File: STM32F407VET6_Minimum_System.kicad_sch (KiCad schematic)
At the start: 20 parts, among them SW1 SW_DIP_x01, U1 STM32F407VET, Y1 8MHz

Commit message: feat: implement sensors schematic
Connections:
- net DHT_DATA_MCU: now reaches U1.84 (PD3)
- net SENS_SCL: now reaches U1.95 (PB8)
- net SENS_SDA: now reaches U1.96 (PB9)
- net BTN1_N: no longer names the net of U1.97 (PE0)
- net BTN2_N: no longer names the net of U1.98 (PE1)
- net LED_1: no longer names the net of U1.1 (PE2)
- net LED_2: no longer names the net of U1.2 (PE3)
- net LED_3: no longer names the net of U1.3 (PE4)
- net LED_4: no longer names the net of U1.4 (PE5)
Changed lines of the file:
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@@
+	(wire
+		(pts
+			(xy 173.99 124.46) (xy 180.34 124.46)
+		)
+		(stroke
+			(width 0)
+			(type default)
+		)
+	)
 	(wire
 		(pts
@@
 	(wire
 		(pts
-			(xy 170.18 86.36) (xy 180.34 86.36)
-		)
-		(stroke
-			(width 0)
-			(type default)
-		)
-	)
-	(wire
-		(pts
 			(xy 167.64 50.8) (xy 180.34 50.8)
 		)
@@
 	(wire
 		(pts
+			(xy 231.14 114.3) (xy 238.76 114.3)
+		)
+		(stroke
+			(width 0)
+			(type default)
+		)
+	)
+	(wire
+		(pts
 			(xy 203.2 34.29) (xy 205.74 34.29)
 		)
@@
 	(wire
 		(pts
-			(xy 170.18 81.28) (xy 180.34 81.28)
-		)
-		(stroke
-			(width 0)
-			(type default)
-		)
-	)
-	(wire
-		(pts
 			(xy 76.2 121.92) (xy 80.01 121.92)
 		)
@@
 	(wire
 		(pts
-			(xy 171.45 73.66) (xy 180.34 73.66)
-		)
-		(stroke
-			(width 0)
-			(type default)
-		)
-	)
-	(wire
-		(pts
 			(xy 331.47 149.86) (xy 331.47 146.05)
 		)
@@
 	(wire
 		(pts
-			(xy 231.14 93.98) (xy 242.57 93.98)
-		)
-		(stroke
-			(width 0)
-			(type default)
-		)
-	)
-	(wire
-		(pts
 			(xy 208.28 185.42) (xy 208.28 189.23)
 		)
@@
 	(wire
 		(pts
-			(xy 170.18 78.74) (xy 180.34 78.74)
-		)
-		(stroke
-			(width 0)
-			(type default)
-		)
-	)
-	(wire
-		(pts
 			(xy 328.93 97.79) (xy 328.93 92.71)
 		)
@@
 	(wire
 		(pts
-			(xy 172.72 111.76) (xy 180.34 111.76)
-		)
-		(stroke
-			(width 0)
-			(type default)
-		)
-	)
-	(wire
-		(pts
 			(xy 96.52 162.56) (xy 104.14 162.56)
 		)
@@
 	(wire
 		(pts
-			(xy 171.45 76.2) (xy 180.34 76.2)
-		)
-		(stroke
-			(width 0)
-			(type default)
-		)
-	)
-	(wire
-		(pts
 			(xy 64.77 121.92) (xy 68.58 121.92)
 		)
@@
 	(wire
 		(pts
-			(xy 170.18 83.82) (xy 180.34 83.82)
-		)
-		(stroke
-			(width 0)
-			(type default)
-		)
-	)
-	(wire
-		(pts
 			(xy 215.9 31.75) (xy 215.9 40.64)
+		)
+		(stroke
+			(width 0)
+			(type default)
+		)
+	)
+	(wire
+		(pts
+			(xy 231.14 116.84) (xy 238.76 116.84)
 		)
 		(stroke
@@
 		)
 	)
+	(label "USB_D_N"
+		(at 242.57 78.74 0)
+		(effects
+			(font
+				(size 1.27 1.27)
+			)
+			(justify left bottom)
+		)
+	)
 	(label "PH1"
 		(at 170.18 68.58 0)
@@
 		)
 	)
-	(global_label "LED_1"
-		(shape input)
-		(at 170.18 78.74 180)
-		(fields_autoplaced yes)
-		(effects
-			(font
-				(size 1.27 1.27)
-			)
-			(justify right)
-		)
-		(property "Intersheetrefs" "${INTERSHEET_REFS}"
-			(at 161.5706 78.74 0)
-			(hide yes)
-			(show_name no)
-			(do_not_autoplace no)
-			(effects
-				(font
-					(size 1.27 1.27)
-				)
-				(justify right)
-			)
+	(label "USB_D_P"
+		(at 242.57 81.28 0)
+		(effects
+			(font
+				(size 1.27 1.27)
+			)
+			(justify left bottom)
 		)
 	)
@@
 		)
 	)
-	(global_label "USB_D_N"
+	(global_label "SENS_SCL"
 		(shape input)
-		(at 242.57 78.74 0)
+		(at 238.76 114.3 0)
 		(fields_autoplaced yes)
 		(effects
@@
 		)
 		(property "Intersheetrefs" "${INTERSHEET_REFS}"
-			(at 253.9009 78.74 0)
+			(at 251.1189 114.3 0)
 			(hide yes)
 			(show_name no)
@@
 				)
 				(justify left)
-			)
-		)
-	)
-	(global_label "BTN1_N"
-		(shape input)
-		(at 171.45 73.66 180)
-		(fields_autoplaced yes)
-		(effects
-			(font
-				(size 1.27 1.27)
-			)
-			(justify right)
-		)
-		(property "Intersheetrefs" "${INTERSHEET_REFS}"
-			(at 161.3891 73.66 0)
-			(hide yes)
-			(show_name no)
-			(do_not_autoplace no)
-			(effects
-				(font
-					(size 1.27 1.27)
-				)
-				(justify right)
-			)
-		)
-	)
-	(global_label "BTN2_N"
-		(shape input)
-		(at 171.45 76.2 180)
-		(fields_autoplaced yes)
-		(effects
-			(font
-				(size 1.27 1.27)
-			)
-			(justify right)
-		)
-		(property "Intersheetrefs" "${INTERSHEET_REFS}"
-			(at 161.3891 76.2 0)
-			(hide yes)
-			(show_name no)
-			(do_not_autoplace no)
-			(effects
-				(font
-					(size 1.27 1.27)
-				)
-				(justify right)
-			)
-		)
-	)
-	(global_label "LED_3"
-		(shape input)
-		(at 170.18 83.82 180)
-		(fields_autoplaced yes)
-		(effects
-			(font
-				(size 1.27 1.27)
-			)
-			(justify right)
-		)
-		(property "Intersheetrefs" "${INTERSHEET_REFS}"
-			(at 161.5706 83.82 0)
-			(hide yes)
-			(show_name no)
-			(do_not_autoplace no)
-			(effects
-				(font
-					(size 1.27 1.27)
-				)
-				(justify right)
 			)
 		)
@@
 		)
 	)
-	(global_label "USB_D_P"
+	(global_label "SENS_SDA"
 		(shape input)
-		(at 242.57 81.28 0)
+		(at 238.76 116.84 0)
 		(fields_autoplaced yes)
 		(effects
@@
 		)
 		(property "Intersheetrefs" "${INTERSHEET_REFS}"
-			(at 253.8404 81.28 0)
+			(at 251.1794 116.84 0)
 			(hide yes)
 			(show_name no)
@@
 		)
 	)
-	(global_label "LED_4"
+	(global_label "DHT_DATA_MCU"
 		(shape input)
-		(at 170.18 86.36 180)
+		(at 173.99 124.46 180)
 		(fields_autoplaced yes)
 		(effects
@@
 		)
 		(property "Intersheetrefs" "${INTERSHEET_REFS}"
-			(at 161.5706 86.36 0)
+			(at 157.0348 124.46 0)
 			(hide yes)
 			(show_name no)
-			(do_not_autoplace no)
-			(effects
-				(font
-					(size 1.27 1.27)
-				)
-				(justify right)
-			)
-		)
-	)
-	(global_label "LED_2"
-		(shape input)
-		(at 170.18 81.28 180)
-		(fields_autoplaced yes)
-		(effects
-			(font
-				(size 1.27 1.27)
-			)
-			(justify right)
-		)
-		(property "Intersheetrefs" "${INTERSHEET_REFS}"
-			(at 161.5706 81.28 0)
-			(hide yes)
-			(show_name no)

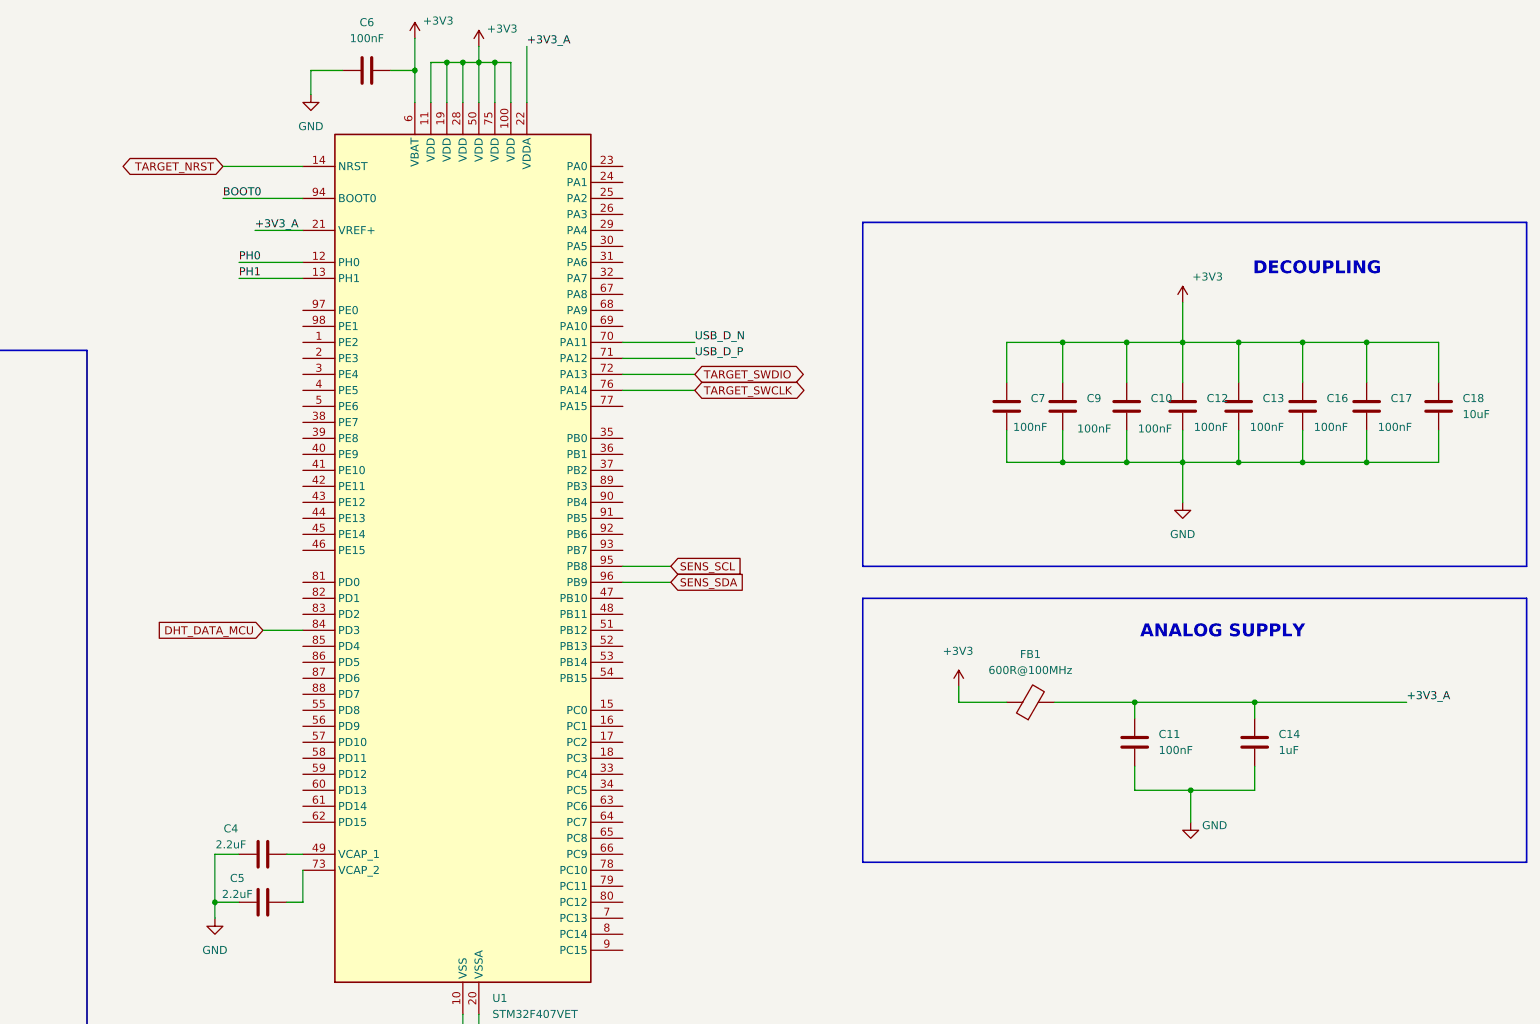
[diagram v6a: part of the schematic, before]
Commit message: feat: implement microSD schematic
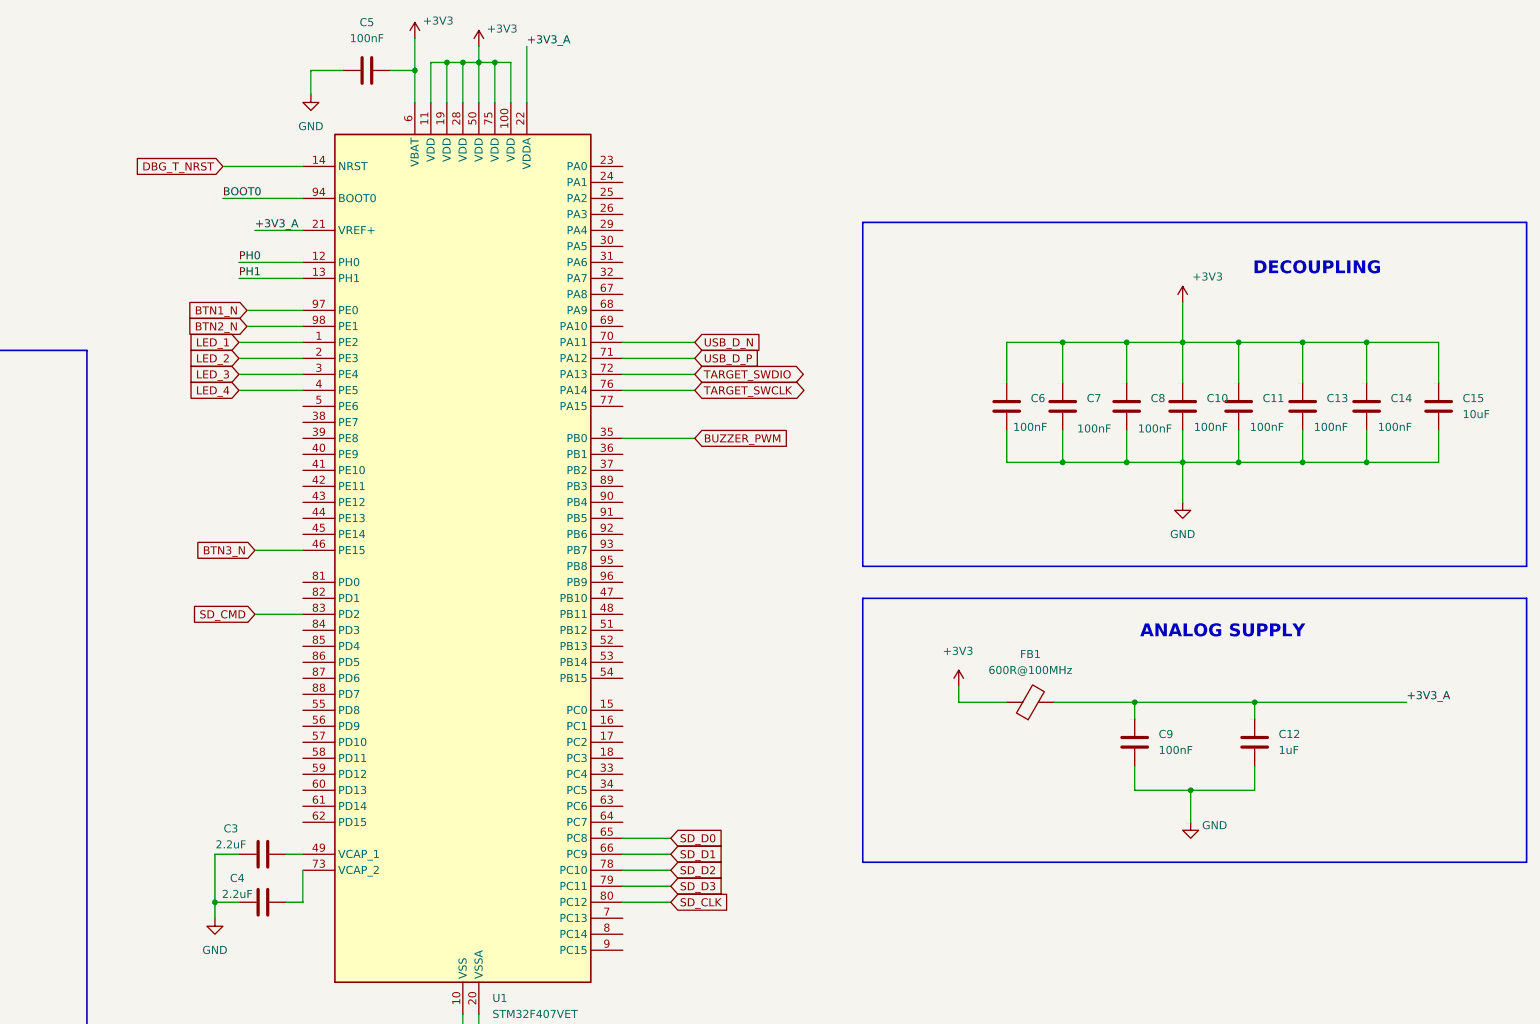
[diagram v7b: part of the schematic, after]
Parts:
- renumbered C12 to C10, C13 to C11, C14 to C12, C16 to C13, C17 to C14, C18 to C15, C4 to C3, C5 to C4, C6 to C5, C7 to C6, C9 to C7, C10 to C8, C11 to C9
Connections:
- net LED_1: now reaches U1.1 (PE2)
- net LED_2: now reaches U1.2 (PE3)
- net LED_3: now reaches U1.3 (PE4)
- net BUZZER_PWM: now reaches U1.35 (PB0)
- net LED_4: now reaches U1.4 (PE5)
- net BTN3_N: now reaches U1.46 (PE15)
- net SD_D0: now reaches U1.65 (PC8)
- net SD_D1: now reaches U1.66 (PC9)
- net SD_D2: now reaches U1.78 (PC10)
- net SD_D3: now reaches U1.79 (PC11)
- net SD_CLK: now reaches U1.80 (PC12)
- net SD_CMD: now reaches U1.83 (PD2)
- net BTN1_N: now reaches U1.97 (PE0)
- net BTN2_N: now reaches U1.98 (PE1)
- net DHT_DATA_MCU: no longer names the net of U1.84 (PD3)
- net SENS_SCL: no longer names the net of U1.95 (PB8)
- net SENS_SDA: no longer names the net of U1.96 (PB9)
- net TARGET_NRST renamed DBG_T_NRST

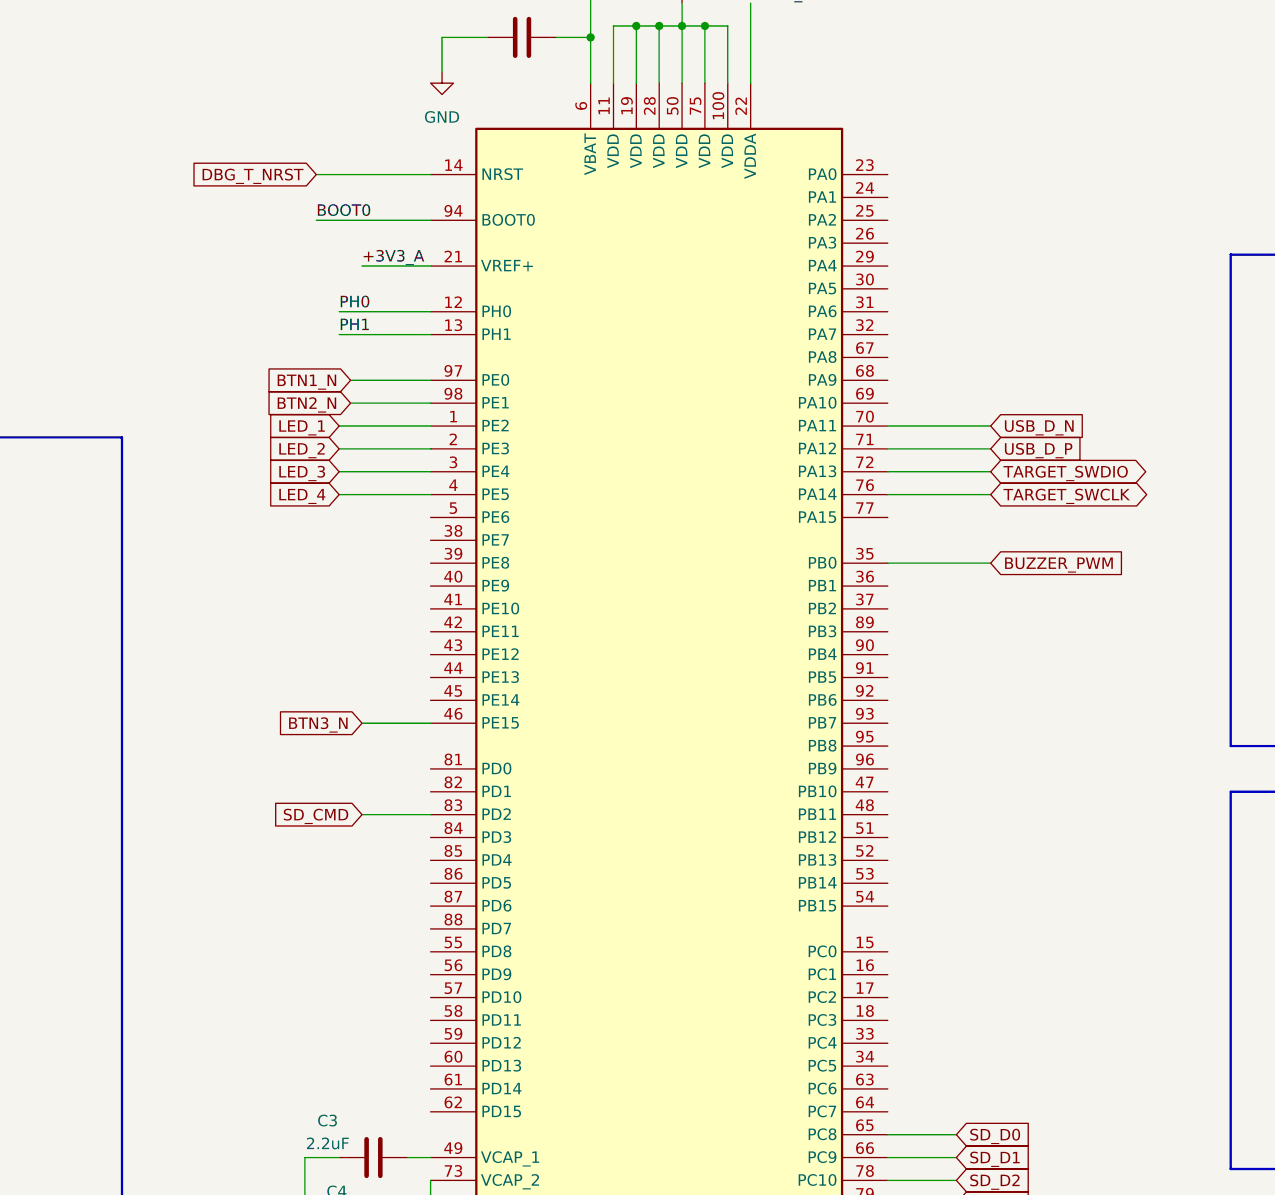
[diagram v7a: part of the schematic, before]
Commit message: feat: add can1 can2 schematic
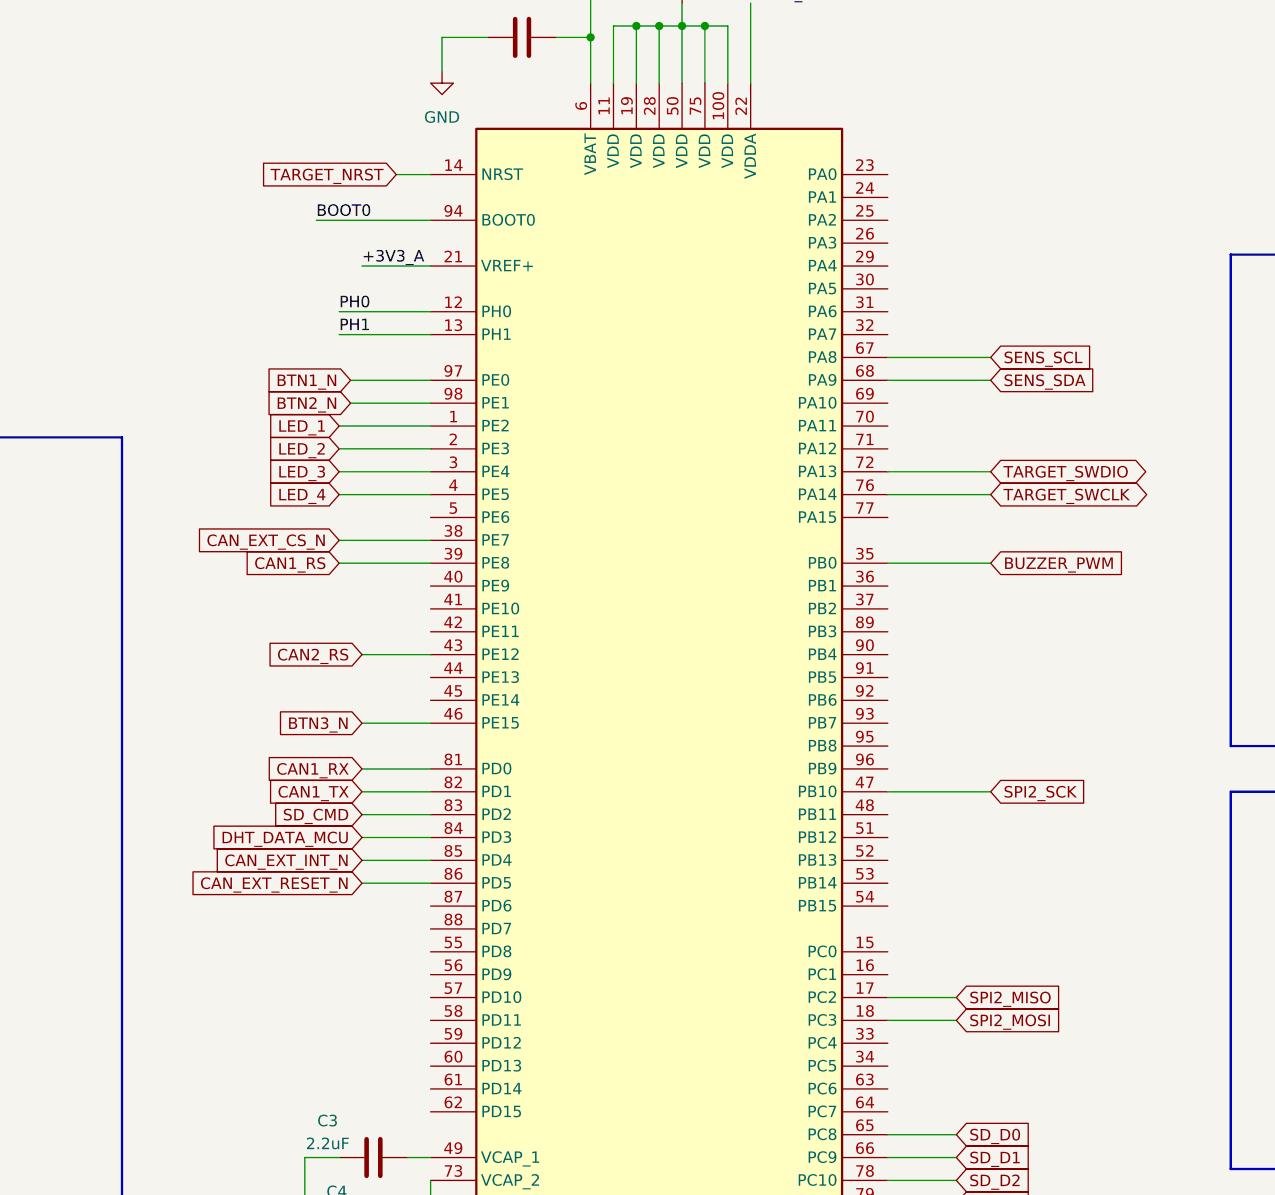
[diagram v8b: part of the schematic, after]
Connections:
- net SPI2_MISO: now reaches U1.17 (PC2)
- net SPI2_MOSI: now reaches U1.18 (PC3)
- net CAN_EXT_CS_N: now reaches U1.38 (PE7)
- net CAN1_RS: now reaches U1.39 (PE8)
- net CAN2_RS: now reaches U1.43 (PE12)
- net SPI2_SCK: now reaches U1.47 (PB10)
- net SENS_SCL: now reaches U1.67 (PA8)
- net SENS_SDA: now reaches U1.68 (PA9)
- net CAN1_RX: now reaches U1.81 (PD0)
- net CAN1_TX: now reaches U1.82 (PD1)
- net DHT_DATA_MCU: now reaches U1.84 (PD3)
- net CAN_EXT_INT_N: now reaches U1.85 (PD4)
- net CAN_EXT_RESET_N: now reaches U1.86 (PD5)
- net DBG_T_NRST renamed TARGET_NRST
- net USB_D_N: no longer names the net of U1.70 (PA11)
- net USB_D_P: no longer names the net of U1.71 (PA12)
